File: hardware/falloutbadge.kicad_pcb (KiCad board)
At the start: 2 copper layers, 82 x 98.1 mm, 105 parts, among them J1 LiPo, J3 USB_C_Receptacle_USB2.0_16P, J4 E-INK, J5 Conn_01x03, Q2 NMOS, Q3 AO3400A, SW1 SW_Push, SW2 SW_Push, SW3 SW_Push, SW4 SW_Push, SW5 SW_Push, T1 BALFLB-WL-09D3, U1 CH592F, U2 STM32WLE5CCUx, U3 CH9102F, U4 USBLC6-2SC6, U5 TP4056, U6 BGS12SN6, U7 AP2112K-3.3, Y1 32MHz, Y2 32MHz

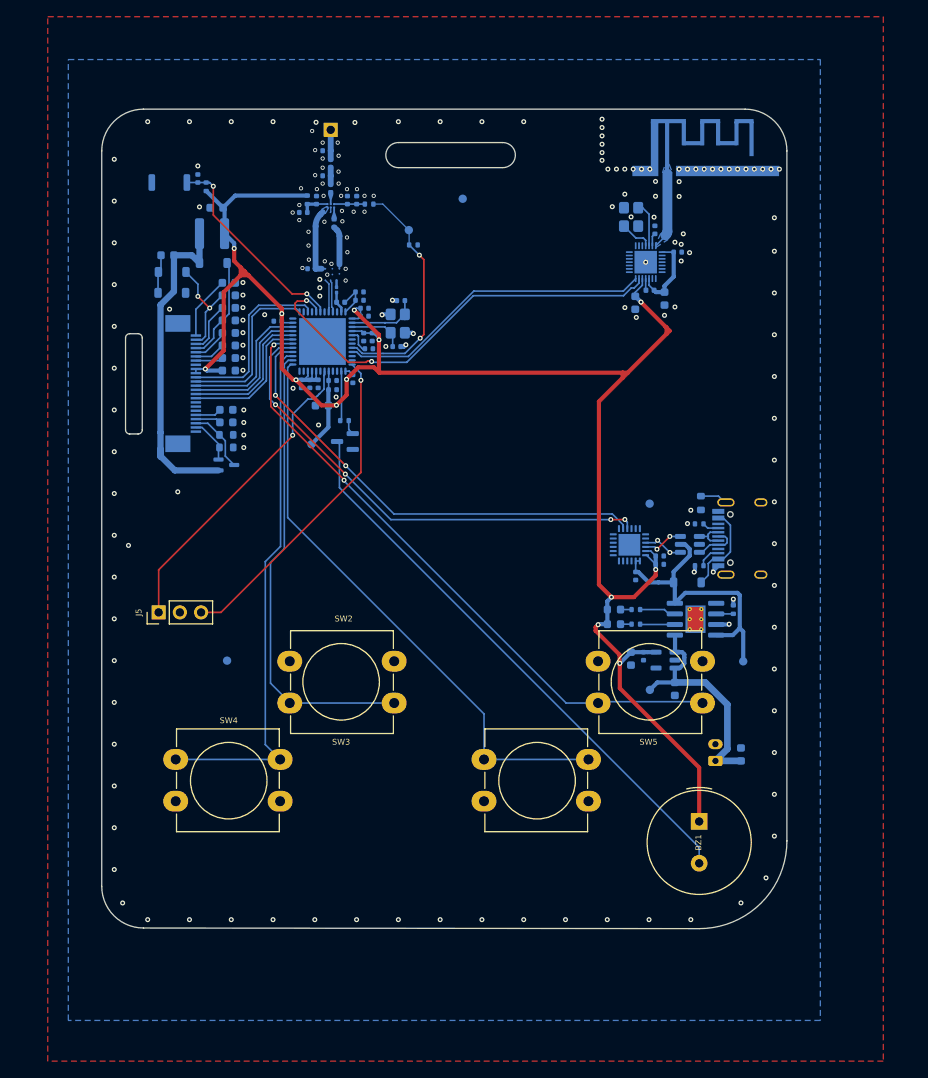
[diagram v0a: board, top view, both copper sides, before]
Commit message: update pcb and improve power path
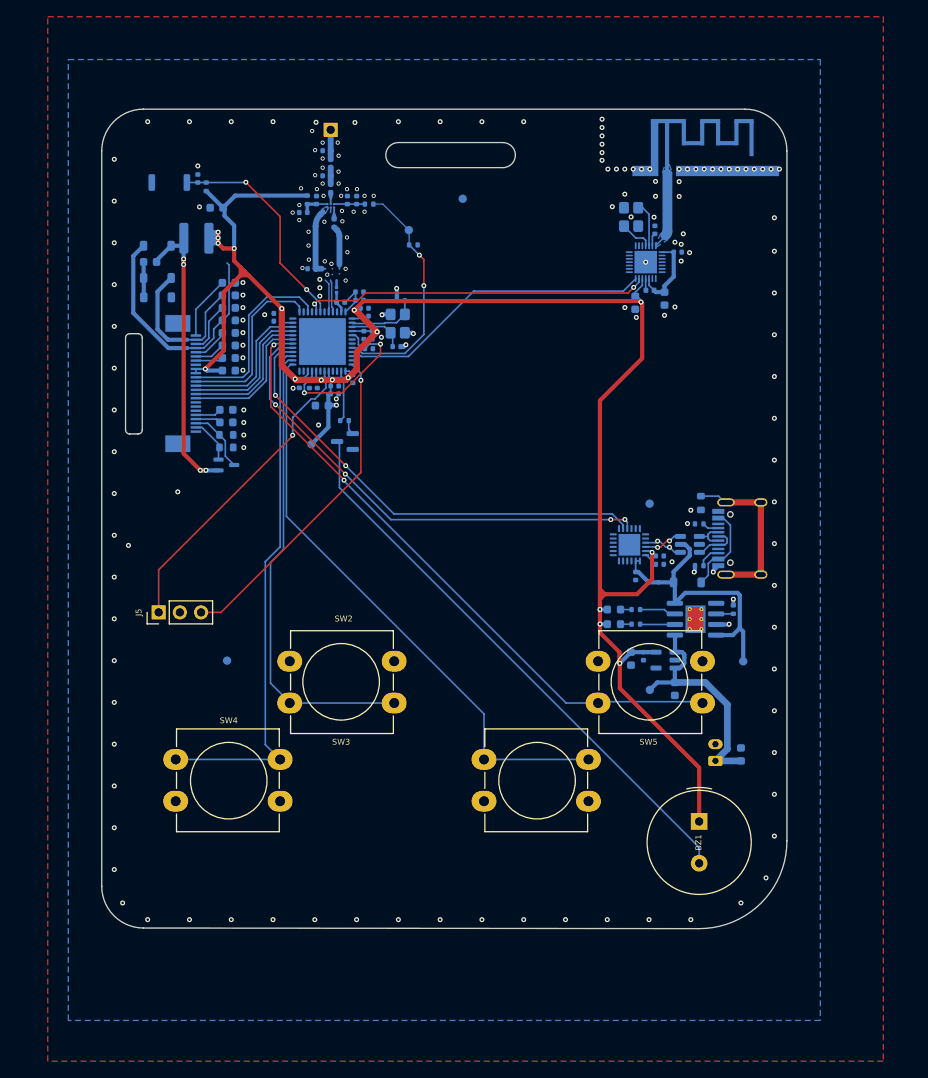
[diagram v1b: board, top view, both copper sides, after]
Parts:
- added C12: 100nF, Capacitor_SMD:C_0402_1005Metric, B.Cu at (130.0, 84.0)
- moved C53 9.26 mm to (126.2, 75.6), turned to 180 degrees
- moved D3 7.01 mm to (111.8, 67.5), turned to 0 degrees
- moved C22 2.23 mm to (110.9, 69.4)
- moved L3 1.95 mm to (116.5, 66.6)
- moved D2 1.91 mm to (111.8, 71.3)
- moved D1 1.79 mm to (111.8, 73.6)
- moved C54 0.69 mm to (133.0, 84.2)
- moved C50 0.55 mm to (133.0, 85.2)
- moved C49 0.25 mm to (128.8, 84.0)
- moved C1 0.23 mm to (136.5, 78.2)
- moved C11 0.23 mm to (137.5, 78.2)
- moved C18 0.10 mm to (130.9, 84.0)
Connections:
- AE3 pad : GND -> (no net)
- AE3 pad 0: GND -> (no net)
- C16 pad 1: Net-(U2-VDDRF1V55) -> /VFBSMPS
- C23 pad 1: +3V3 -> Net-(U3-V3)
- U2 pad 29: Net-(U2-VDDRF1V55) -> /VFBSMPS
- U2 pad 45: +3V3 -> /VFBSMPS
- U3 pad 6: +3V3 -> Net-(U3-V3)
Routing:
- net /VFBSMPS: track 0.00 -> 20.1 mm, vias 0 -> 2
- net /PREVGH: track 12.5 -> 30.3 mm
- net Net-(J3-SHIELD): track 3.31 -> 20.3 mm
- net /UART1_RX: track 52.6 -> 41.4 mm
- net /PREVGL: track 12.6 -> 19.0 mm, vias 2 -> 0
- net +3V3: track 234.5 -> 237.8 mm, vias 13 -> 18
- net Net-(D3-A): track 40.2 -> 37.0 mm, vias 0 -> 4
- net Net-(U2-VDDRF1V55): track 2.79 -> 0.00 mm
- net Net-(U3-V3): track 0.00 -> 1.66 mm
- net Net-(U2-NRST): track 24.8 -> 26.3 mm
- net /SPI_SCK: track 20.2 -> 21.3 mm
- net /SPI_MOSI: track 21.5 -> 22.5 mm
- net GND: track 10.3 -> 11.3 mm

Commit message: stitching vias + drc
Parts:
- moved SW2 1.01 mm to (150.3, 129.8)
- moved SW4 1.00 mm to (114.0, 129.9)
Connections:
- AE3 pad : (no net) -> GND
- AE3 pad 0: (no net) -> GND
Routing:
- net /PB5: track 63.3 -> 64.3 mm
- net /PB3: track 70.0 -> 70.6 mm
- net GND: vias 177 -> 263

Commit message: final fixes
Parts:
- removed U5: TP4056, Package_SO:SOIC-8-1EP_3.9x4.9mm_P1.27mm_EP2.41x3.3mm_ThermalVias
- added U8: TP4056-42-ESOP8, Package_SO:SOIC-8-1EP_3.9x4.9mm_P1.27mm_EP2.41x3.3mm_ThermalVias, B.Cu at (176.3, 112.2)
- AE3: footprint antenna:ANT-F-1-2.4G-1.6mmFR4-WCH -> antenna:ANT-F-1-2.4G-0.8mmFR4-WCH
- C20, C22: footprint Capacitor_SMD:C_0603_1608Metric -> Capacitor_SMD:C_1206_3216Metric
- C42, C46: value 10uF -> 4.7uF
- C5, C6: value 20pF -> 6.8pF
- D1, D2, D3: value D -> MBR0530
- D4: footprint Diode_SMD:D_SOD-123 -> Diode_SMD:D_SOD-123F
- D8: value GREEN -> NOT RED
- FB1: footprint Resistor_SMD:R_0603_1608Metric -> Inductor_SMD:L_0805_2012Metric
- L1: value 47nH -> 68nH
- L3: footprint Inductor_SMD:L_APV_ANR4018 -> Inductor_SMD:L_Changjiang_FNR6028S
- L6: footprint Inductor_SMD:L_0402_1005Metric -> Inductor_SMD:L_1210_3225Metric
- Q2: value NMOS -> Si1308EDL
- R12, R13: value 1k -> 330R
- R6, R7: footprint Resistor_SMD:R_0603_1608Metric -> Resistor_SMD:R_0402_1005Metric
- SW1: footprint Button_Switch_SMD:SW_Push_SPST_NO_Alps_SKRK -> Button_Switch_SMD:SW_SPST_TS-1088-xR025
- SW2, SW3, SW4, SW5: footprint Button_Switch_THT:SW_PUSH-12mm_Wuerth-430476085716 -> Button_Switch_THT:SW_PUSH-12mm
- moved D3 34.5 mm to (110.6, 102.0)
- moved L3 34.5 mm to (116.7, 101.1), turned to -90 degrees
- moved C22 30.1 mm to (110.8, 99.5)
- moved D2 25.5 mm to (110.9, 96.8)
- moved C33 24.3 mm to (120.5, 96.2)
- moved C32 21.3 mm to (120.5, 94.7)
- moved D1 20.9 mm to (110.9, 94.5)
- moved Q2 20.8 mm to (119.2, 72.9)
- moved C31 18.3 mm to (120.5, 93.2)
- moved R6 15.8 mm to (119.6, 75.8)
- moved C30 15.3 mm to (120.5, 91.7)
- moved R7 13.1 mm to (119.6, 77.0)
- moved C29 12.3 mm to (120.5, 90.2)
- moved C25 10.3 mm to (120.2, 78.3)
- moved AE3 9.75 mm to (182.0, 54.5)
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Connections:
- C25 pad 2: Net-(J4-Pin_4) -> Net-(J4-Pin_21)
- C26 pad 2: Net-(J4-Pin_5) -> Net-(J4-Pin_20)
- C27 pad 2: Net-(J4-Pin_18) -> Net-(J4-Pin_7)
- C28 pad 2: Net-(J4-Pin_19) -> Net-(J4-Pin_6)
- C29 pad 2: Net-(J4-Pin_20) -> Net-(J4-Pin_5)
- C31 pad 2: Net-(J4-Pin_22) -> Net-(J4-Pin_3)
- C33 pad 2: Net-(J4-Pin_24) -> Net-(J4-Pin_1)
- J4 pad 1: unconnected-(J4-Pin_1-Pad1) -> Net-(J4-Pin_1)
- J4 pad 10: /RST -> +3V3
- J4 pad 11: /DC -> /SPI_MOSI
- J4 pad 12: /CS -> /SPI_SCK
- J4 pad 13: /SPI_SCK -> /CS
- J4 pad 14: /SPI_MOSI -> /DC
- J4 pad 15: +3V3 -> /RST
- J4 pad 16: +3V3 -> /BUSY
- J4 pad 18: Net-(J4-Pin_18) -> unconnected-(J4-Pin_18-Pad18)
- J4 pad 19: Net-(J4-Pin_19) -> unconnected-(J4-Pin_19-Pad19)
- J4 pad 2: /GDR -> /PREVGL
- J4 pad 21: /PREVGH -> Net-(J4-Pin_21)
- J4 pad 22: Net-(J4-Pin_22) -> /RESE
- J4 pad 23: /PREVGL -> /GDR
- J4 pad 24: Net-(J4-Pin_24) -> unconnected-(J4-Pin_24-Pad24)
- J4 pad 3: /RESE -> Net-(J4-Pin_3)
- J4 pad 4: Net-(J4-Pin_4) -> /PREVGH
- J4 pad 6: unconnected-(J4-Pin_6-Pad6) -> Net-(J4-Pin_6)
- J4 pad 7: unconnected-(J4-Pin_7-Pad7) -> Net-(J4-Pin_7)
- J4 pad 9: /BUSY -> +3V3
- U2 pad 10: /CS -> /BUSY
- U2 pad 7: /BUSY -> /CS
- U2 pad 8: /RST -> /DC
- U2 pad 9: /DC -> /RST
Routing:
- net +3V3: track 237.8 -> 261.0 mm
- net Net-(J4-Pin_1): track 0.00 -> 8.09 mm
- net Net-(J4-Pin_24): track 7.90 -> 0.00 mm
- net Net-(J4-Pin_3): track 0.00 -> 6.45 mm
- net Net-(J4-Pin_22): track 6.13 -> 0.00 mm
- net /PREVGH: track 30.3 -> 24.9 mm
- net Net-(J4-Pin_6): track 0.00 -> 3.98 mm
- net Net-(J4-Pin_19): track 3.71 -> 0.00 mm
- net Net-(J4-Pin_7): track 0.00 -> 3.57 mm
- net Net-(J4-Pin_21): track 0.00 -> 3.55 mm
- net VBUS: track 35.2 -> 38.7 mm
- net /VDCIA: track 9.62 -> 13.0 mm
- net /CS: track 17.0 -> 13.7 mm
- net /UART1_TX: track 38.0 -> 41.3 mm
- net Net-(J4-Pin_18): track 3.30 -> 0.00 mm
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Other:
- board size 82 x 98.1 mm -> 86 x 98 mm

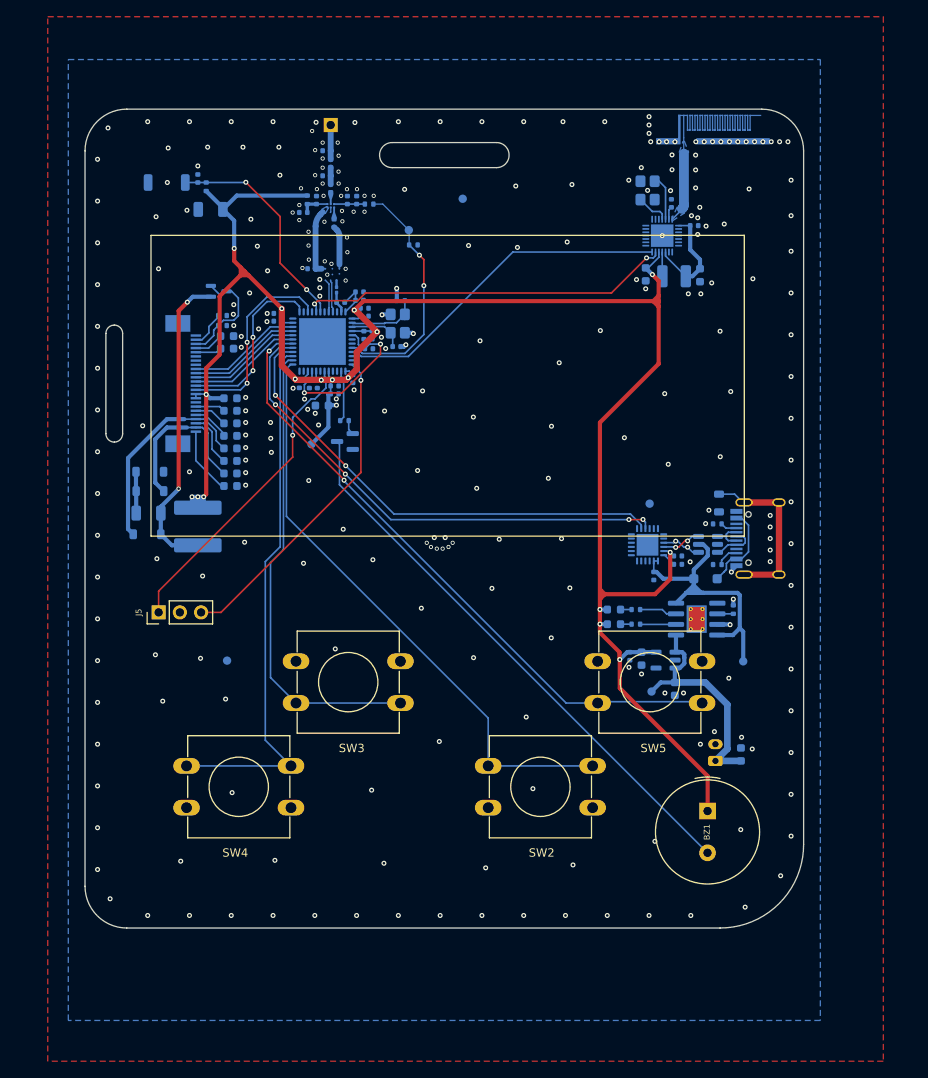
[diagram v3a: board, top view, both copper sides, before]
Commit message: assign lcsc parts and flip eink
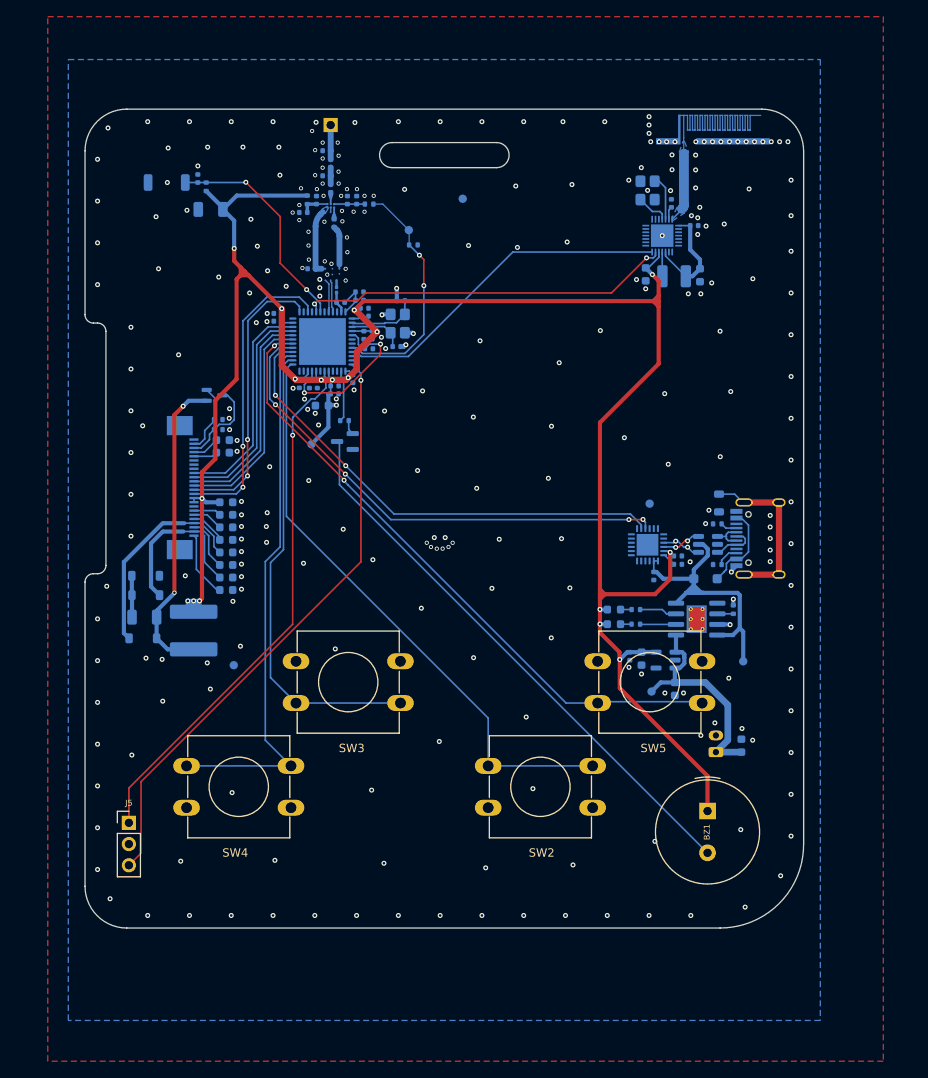
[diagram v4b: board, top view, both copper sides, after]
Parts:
- J4: footprint falloutbadge:FPC-SMD_24P-P0.50_05B20U24P -> Connector_FFC-FPC:TE_2-1734839-4_1x24-1MP_P0.5mm_Horizontal
- moved J5 25.4 mm to (108.4, 136.5), turned to 0 degrees
- moved C22 12.5 mm to (110.2, 111.9)
- moved C24 12.5 mm to (120.0, 98.2)
- moved C25 12.5 mm to (119.7, 90.7)
- moved C26 12.5 mm to (119.7, 92.2)
- moved C27 12.5 mm to (120.0, 99.7)
- moved C28 12.5 mm to (120.0, 101.2)
- moved C29 12.5 mm to (120.0, 102.7)
- moved C30 12.5 mm to (120.0, 104.2)
- moved C31 12.5 mm to (120.0, 105.7)
- moved C32 12.5 mm to (120.0, 107.2)
- moved C33 12.5 mm to (120.0, 108.7)
- moved D1 12.5 mm to (110.4, 107.0)
- moved D2 12.5 mm to (110.4, 109.3)
- moved D3 12.5 mm to (110.1, 114.5)
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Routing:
- net /SWDIO: track 39.4 -> 71.9 mm
- net /SWCLK: track 37.5 -> 64.1 mm
- net /BUSY: track 13.7 -> 26.3 mm
- net /RST: track 13.7 -> 26.3 mm
- net /DC: track 13.7 -> 26.3 mm
- net /CS: track 13.7 -> 26.3 mm
- net /SPI_MOSI: track 23.8 -> 36.2 mm
- net +3V3: track 261.0 -> 273.4 mm
- net /SPI_SCK: track 21.3 -> 33.7 mm
- net +BATT: track 28.5 -> 27.5 mm
- net GND: vias 278 -> 282
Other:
- outline, holes or cut-outs redrawn
